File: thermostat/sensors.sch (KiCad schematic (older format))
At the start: 8 parts

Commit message: Moved I2C peripherals into one schematic, moved GPIO peripherals onto main schematic.
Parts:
- added C?: 10n, Capacitor_SMD:C_0603_1608Metric, symbol Device:C
- added R? (x2): 4k7, symbol Device:R
- added U?: AT24C512, Package_DIP:DIP-8_W7.62mm_SMDSocket_SmallPads, symbol Memory_EEPROM:CAT24C256
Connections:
- wire segments 44 -> 71
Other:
- note added: "EEPROM for off-ESP config"
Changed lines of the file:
@@
 $Descr A4 11693 8268
 encoding utf-8
-Sheet 4 4
+Sheet 3 4
 Title ""
 Date ""
@@
 MKW41Z also has RTC but no battery backup for power loss.\nWe do not need interrupt out since MKW41Z has that in its own RTC\n
 NoConn ~ 4050 3700
-Text HLabel 4150 5150 0    50   Input ~ 0
+Text HLabel 4100 5700 0    50   Input ~ 0
 SCL
-Text HLabel 4150 5250 0    50   Input ~ 0
+Text HLabel 4100 5800 0    50   Input ~ 0
 SDA
-Wire Wire Line
-	4150 5150 4350 5150
-Wire Wire Line
-	4350 5250 4150 5250
-Text Label 4350 5150 2    50   ~ 0
+Text Label 5250 5700 2    50   ~ 0
 SCL
-Text Label 4350 5250 2    50   ~ 0
+Text Label 5250 5800 2    50   ~ 0
 SDA
+$Comp
+L Memory_EEPROM:CAT24C256 U?
+U 1 1 5F42FF23
+P 10000 4200
+AR Path="/5F42FF23" Ref="U?"  Part="1"
+AR Path="/5F32546C/5F42FF23" Ref="U?"  Part="1"
+F 0 "U?" H 9750 4450 50  0000 C CNN
+F 1 "AT24C512" H 10250 4450 50  0000 C CNN
+F 2 "Package_DIP:DIP-8_W7.62mm_SMDSocket_SmallPads" H 10000 4200 50  0001 C CNN
+F 3 "https://www.onsemi.cn/PowerSolutions/document/CAT24C256-D.PDF" H 10000 4200 50  0001 C CNN
+	1    10000 4200
+	1    0    0    -1
+$EndComp
+$Comp
+L Device:C C?
+U 1 1 5F42FF29
+P 9750 3800
+AR Path="/5F42FF29" Ref="C?"  Part="1"
+AR Path="/5F32546C/5F42FF29" Ref="C?"  Part="1"
+F 0 "C?" V 9498 3800 50  0000 C CNN
+F 1 "10n" V 9589 3800 50  0000 C CNN
+F 2 "Capacitor_SMD:C_0603_1608Metric" H 9788 3650 50  0001 C CNN
+F 3 "~" H 9750 3800 50  0001 C CNN
+	1    9750 3800
+	0    1    1    0
+$EndComp
+$Comp
+L power:+3V3 #PWR?
+U 1 1 5F42FF2F
+P 10000 3700
+AR Path="/5F42FF2F" Ref="#PWR?"  Part="1"
+AR Path="/5F32546C/5F42FF2F" Ref="#PWR?"  Part="1"
+F 0 "#PWR?" H 10000 3550 50  0001 C CNN
+F 1 "+3V3" H 10015 3873 50  0000 C CNN
+F 2 "" H 10000 3700 50  0001 C CNN
+F 3 "" H 10000 3700 50  0001 C CNN
+	1    10000 3700
+	1    0    0    -1
+$EndComp
+Wire Wire Line
+	10000 3700 10000 3800
+Wire Wire Line
+	9900 3800 10000 3800
+Connection ~ 10000 3800
+Wire Wire Line
+	10000 3800 10000 3900
+$Comp
+L power:GND #PWR?
+U 1 1 5F42FF39
+P 9550 3800
+AR Path="/5F42FF39" Ref="#PWR?"  Part="1"
+AR Path="/5F32546C/5F42FF39" Ref="#PWR?"  Part="1"
+F 0 "#PWR?" H 9550 3550 50  0001 C CNN
+F 1 "GND" V 9555 3672 50  0000 R CNN
+F 2 "" H 9550 3800 50  0001 C CNN
+F 3 "" H 9550 3800 50  0001 C CNN
+	1    9550 3800
+	0    1    1    0
+$EndComp
+Wire Wire Line
+	9550 3800 9600 3800
+Wire Wire Line
+	9550 4100 9550 4200
+Wire Wire Line
+	9550 4550 10000 4550
+Wire Wire Line
+	10450 4550 10450 4300
+Wire Wire Line
+	10450 4300 10400 4300
+Wire Wire Line
+	10000 4500 10000 4550
+Connection ~ 10000 4550
+Wire Wire Line
+	10000 4550 10450 4550
+Wire Wire Line
+	9550 4100 9600 4100
+Wire Wire Line
+	9600 4200 9550 4200
+Connection ~ 9550 4200
+Wire Wire Line
+	9550 4200 9550 4300
+Wire Wire Line
+	9600 4300 9550 4300
+Connection ~ 9550 4300
+Wire Wire Line
+	9550 4300 9550 4550
+$Comp
+L power:GND #PWR?
+U 1 1 5F42FF4E
+P 10000 4600
+AR Path="/5F42FF4E" Ref="#PWR?"  Part="1"
+AR Path="/5F32546C/5F42FF4E" Ref="#PWR?"  Part="1"
+F 0 "#PWR?" H 10000 4350 50  0001 C CNN
+F 1 "GND" H 10005 4427 50  0000 C CNN
+F 2 "" H 10000 4600 50  0001 C CNN
+F 3 "" H 10000 4600 50  0001 C CNN
+	1    10000 4600
+	1    0    0    -1
+$EndComp
+Wire Wire Line
+	10000 4600 10000 4550
+Text Notes 9450 3450 0    50   ~ 0
+EEPROM for off-ESP config
+Wire Notes Line
+	10600 3300 10600 4850
+Wire Notes Line
+	10600 4850 9200 4850
+Wire Notes Line
+	9200 4850 9200 3300
+Wire Notes Line
+	9200 3300 10600 3300
+Text Label 10550 4100 2    50   ~ 0
+SDA
+Wire Wire Line
+	10550 4100 10400 4100
+Text Label 10550 4200 2    50   ~ 0
+SCL
+Wire Wire Line
+	10550 4200 10400 4200
+$Comp
+L Device:R R?
+U 1 1 5F430FFF
+P 4500 5500
+F 0 "R?" H 4570 5546 50  0000 L CNN
+F 1 "4k7" H 4570 5455 50  0000 L CNN
+F 2 "" V 4430 5500 50  0001 C CNN
+F 3 "~" H 4500 5500 50  0001 C CNN
+	1    4500 5500
+	1    0    0    -1
+$EndComp
+$Comp
+L Device:R R?
+U 1 1 5F431377
+P 4850 5500
+F 0 "R?" H 4920 5546 50  0000 L CNN
+F 1 "4k7" H 4920 5455 50  0000 L CNN
+F 2 "" V 4780 5500 50  0001 C CNN
+F 3 "~" H 4850 5500 50  0001 C CNN
+	1    4850 5500
+	1    0    0    -1
+$EndComp
+Wire Wire Line
+	4100 5700 4500 5700
+Wire Wire Line
+	4100 5800 4850 5800
+Wire Wire Line
+	4500 5650 4500 5700
+Connection ~ 4500 5700
+Wire Wire Line
+	4500 5700 5250 5700
+Wire Wire Line
+	4850 5650 4850 5800
+Connection ~ 4850 5800
+Wire Wire Line
+	4850 5800 5250 5800
+$Comp
+L power:+3V3 #PWR?
+U 1 1 5F436E27
+P 4700 5250
+AR Path="/5E9313E4/5F436E27" Ref="#PWR?"  Part="1"
+AR Path="/5F436E27" Ref="#PWR?"  Part="1"
+AR Path="/5F32546C/5F436E27" Ref="#PWR?"  Part="1"
+F 0 "#PWR?" H 4700 5100 50  0001 C CNN
+F 1 "+3V3" H 4715 5423 50  0000 C CNN
+F 2 "" H 4700 5250 50  0001 C CNN
+F 3 "" H 4700 5250 50  0001 C CNN
+	1    4700 5250
+	1    0    0    -1
+$EndComp
+Wire Wire Line
+	4500 5350 4500 5300
+Wire Wire Line
+	4500 5300 4700 5300
+Wire Wire Line
+	4850 5300 4850 5350
+Wire Wire Line
+	4700 5250 4700 5300
+Connection ~ 4700 5300
+Wire Wire Line
+	4700 5300 4850 5300
 $EndSCHEMATC

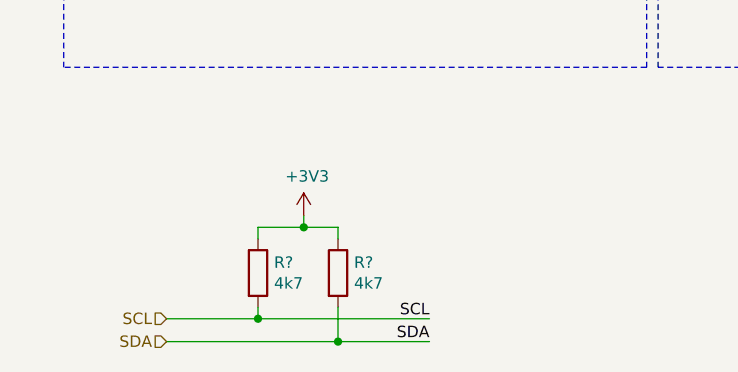
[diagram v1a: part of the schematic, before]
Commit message: Put LEDs and GPIOs into separate schematic, GPIO for arrow buttons are now attached over an expander.
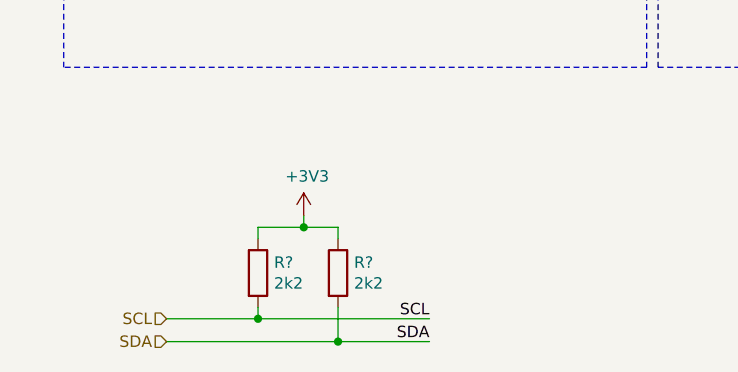
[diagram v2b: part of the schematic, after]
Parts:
- R? (x2): value 4k7 -> 2k2
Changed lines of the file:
@@
 $Descr A4 11693 8268
 encoding utf-8
-Sheet 3 4
+Sheet 3 5
 Title ""
 Date ""
@@
 P 4500 5500
 F 0 "R?" H 4570 5546 50  0000 L CNN
-F 1 "4k7" H 4570 5455 50  0000 L CNN
+F 1 "2k2" H 4570 5455 50  0000 L CNN
 F 2 "" V 4430 5500 50  0001 C CNN
 F 3 "~" H 4500 5500 50  0001 C CNN
@@
 P 4850 5500
 F 0 "R?" H 4920 5546 50  0000 L CNN
-F 1 "4k7" H 4920 5455 50  0000 L CNN
+F 1 "2k2" H 4920 5455 50  0000 L CNN
 F 2 "" V 4780 5500 50  0001 C CNN
 F 3 "~" H 4850 5500 50  0001 C CNN

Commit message: Fixed orphaned symbols after Kicad library update. Kinetis MCU is now in upstream, thanks to me :)
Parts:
- removed U?: MCP7940N-xMS, Package_SO:MSOP-8_3x3mm_P0.65mm, symbol Timer:MCP7940N-xMS
- added U?: MCP7940N-xMS, symbol Timer_RTC:MCP7940N-xMS
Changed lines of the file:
@@
 	6950 2950 6950 3050
-$Comp
-L Timer:MCP7940N-xMS U?
-U 1 1 5F32A0E7
-P 4450 3600
-AR Path="/5F32A0E7" Ref="U?"  Part="1"
-AR Path="/5F32546C/5F32A0E7" Ref="U?"  Part="1"
-F 0 "U?" H 4150 3250 50  0000 C CNN
-F 1 "MCP7940N-xMS" H 4800 3250 50  0000 C CNN
-F 2 "Package_SO:MSOP-8_3x3mm_P0.65mm" H 4450 3600 50  0001 C CNN
-F 3 "http://ww1.microchip.com/downloads/en/DeviceDoc/20005010F.pdf" H 4450 3600 50  0001 C CNN
-	1    4450 3600
-	1    0    0    -1
-$EndComp
 $Comp
 L Sensor_Temperature:MCP9844x-xMN U?
@@
 Wire Wire Line
 	4700 5300 4850 5300
+$Comp
+L Timer_RTC:MCP7940N-xMS U?
+U 1 1 5F69CF88
+P 4450 3600
+F 0 "U?" H 4200 3250 50  0000 C CNN
+F 1 "MCP7940N-xMS" H 4800 3250 50  0000 C CNN
+F 2 "" H 4450 3600 50  0001 C CNN
+F 3 "http://ww1.microchip.com/downloads/en/DeviceDoc/20005010F.pdf" H 4450 3600 50  0001 C CNN
+	1    4450 3600
+	1    0    0    -1
+$EndComp
 $EndSCHEMATC

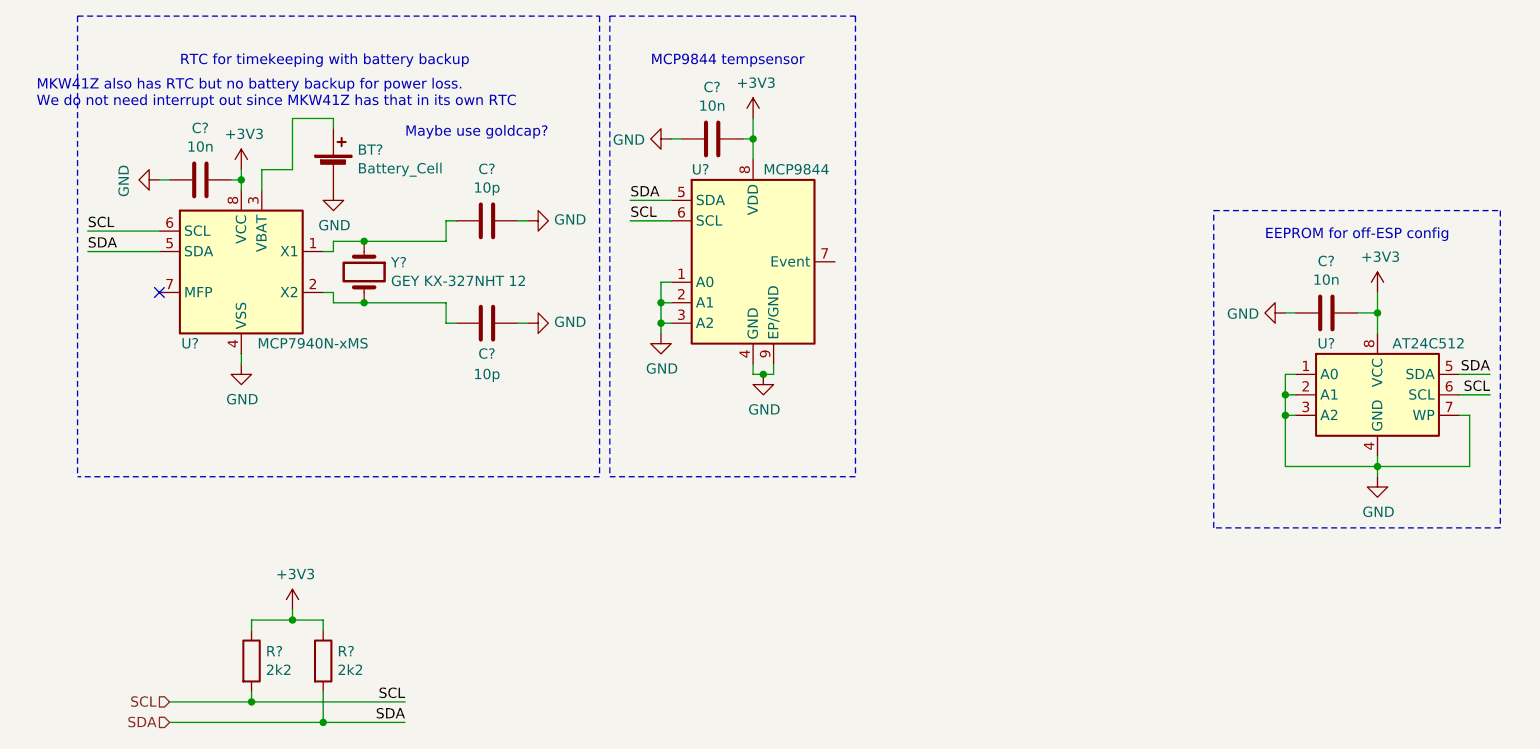
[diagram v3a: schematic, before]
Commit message: Updated symbols after library update, some footprints still need to be assigned. Deleted PCB except for Display and buttons. Button arrangement wrong. Move buttons to other side of Display. Maybe put buttons on separate PCB and create one PCB for MCU and logic, since that needs to be a four layer one. That is expensive and should be kept as small as possible.
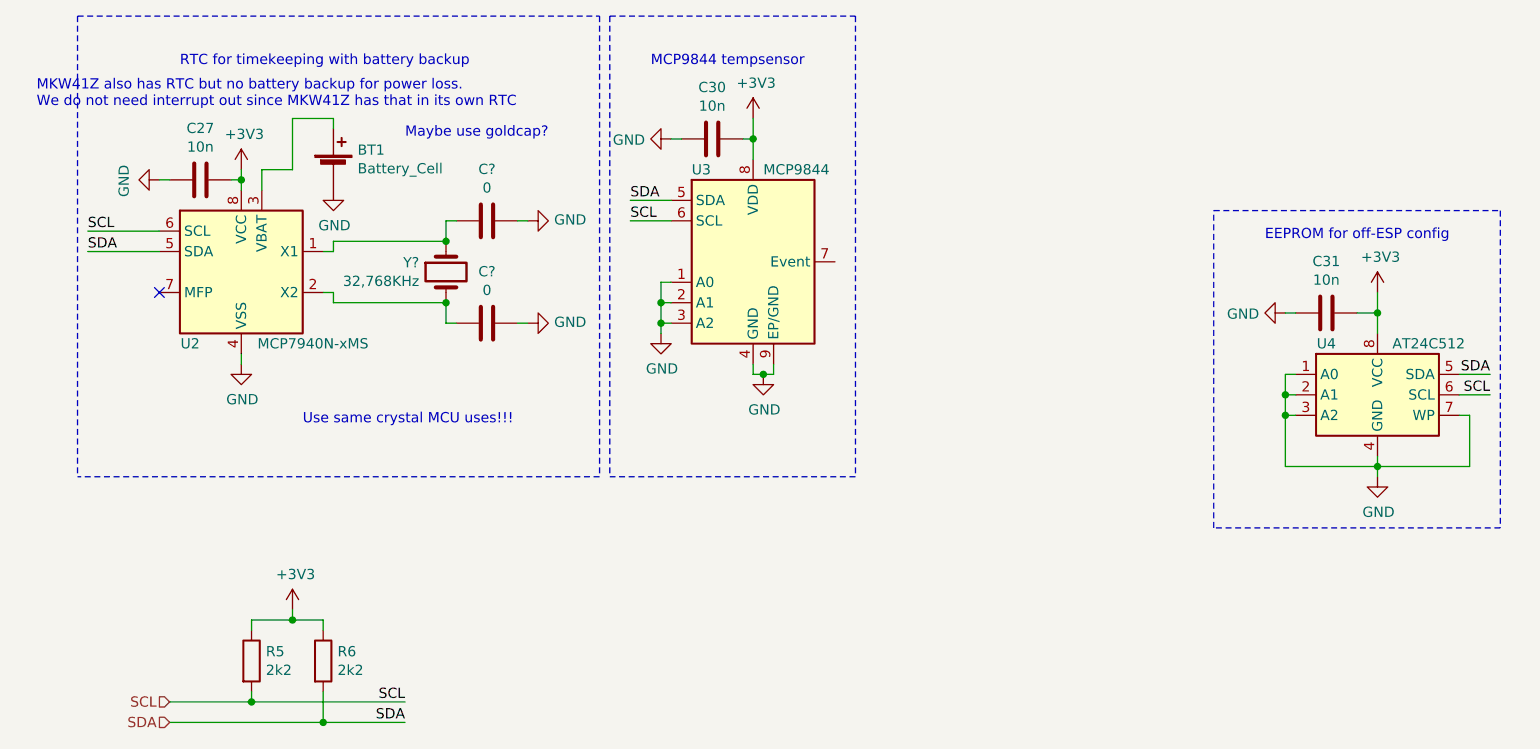
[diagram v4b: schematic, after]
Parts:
- removed C? (x2): 10p, Capacitor_SMD:C_0603_1608Metric, symbol Device:C
- removed Y?: GEY KX-327NHT 12, Crystal:Crystal_SMD_3215-2Pin_3.2x1.5mm, symbol Device:Crystal
- added C? (x2): 0, Capacitor_SMD:C_0603_1608Metric, symbol Device:C
- added Y?: 32,768KHz, symbol Device:Crystal
- R5, R6: renamed from R?; footprint (none) -> Resistor_SMD:R_0603_1608Metric
- U2: renamed from U?; footprint (none) -> Package_SO:MSOP-8_3x3mm_P0.65mm
- gave numbers to parts that had none: 6
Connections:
- net GND: now also C?.1, C?.1
- net at U2.1 (X1): now also C?.2, Y?.1
- net at U2.2 (X2): now also C?.2, Y?.2
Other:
- note added: "Use same crystal MCU uses!!!"

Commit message: Finalized Thermostat circuit based on the MKW41Z.
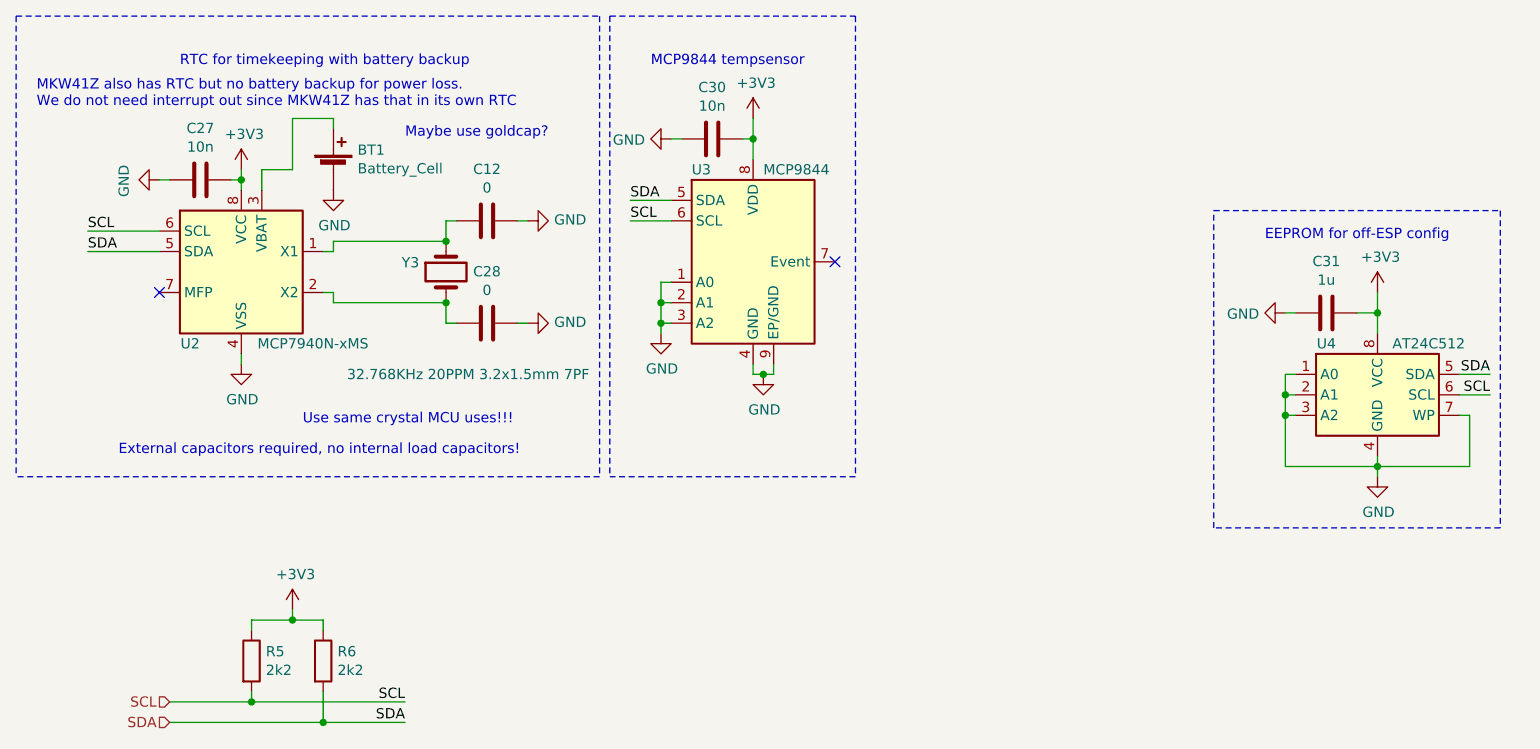
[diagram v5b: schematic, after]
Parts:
- C31: value 10n -> 1u
- Y3: renamed from Y?; value 32,768KHz -> 32.768KHz 20PPM 3.2x1.5mm 7PF; footprint (none) -> Crystal:Crystal_SMD_3215-2Pin_3.2x1.5mm
- gave numbers to parts that had none: 2
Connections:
- no-connect marks 1 -> 2
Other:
- note added: "External capacitors required, no internal load capacitors!"
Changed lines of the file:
@@
 RTC for timekeeping with battery backup
 Wire Notes Line
-	3650 2350 6200 2350
+	3350 2350 6200 2350
 Wire Notes Line
 	6200 2350 6200 4600
@@
 	6250 2350 6250 4600
 Wire Notes Line
-	3650 2350 3650 4600
-Wire Notes Line
-	6200 4600 3650 4600
+	3350 2350 3350 4600
+Wire Notes Line
+	6200 4600 3350 4600
 $Comp
 L Device:C C?
@@
 AR Path="/5F32546C/5F42FF29" Ref="C31"  Part="1"
 F 0 "C31" V 9498 3800 50  0000 C CNN
-F 1 "10n" V 9589 3800 50  0000 C CNN
+F 1 "1u" V 9589 3800 50  0000 C CNN
 F 2 "Capacitor_SMD:C_0603_1608Metric" H 9788 3650 50  0001 C CNN
 F 3 "~" H 9750 3800 50  0001 C CNN
@@
 P 5450 3600
 AR Path="/5F6FEFA4" Ref="Y?"  Part="1"
-AR Path="/5F32546C/5F6FEFA4" Ref="Y?"  Part="1"
-F 0 "Y?" V 5404 3731 50  0000 L CNN
-F 1 "32,768KHz" V 5495 3731 50  0000 L CNN
-F 2 "" H 5450 3600 50  0001 C CNN
+AR Path="/5F32546C/5F6FEFA4" Ref="Y3"  Part="1"
+F 0 "Y3" V 5404 3731 50  0000 L CNN
+F 1 "32.768KHz 20PPM 3.2x1.5mm 7PF" V 5950 2900 50  0000 L CNN
+F 2 "Crystal:Crystal_SMD_3215-2Pin_3.2x1.5mm" H 5450 3600 50  0001 C CNN
 F 3 "~" H 5450 3600 50  0001 C CNN
 	1    5450 3600
@@
 P 5650 3350
 AR Path="/5F70128F" Ref="C?"  Part="1"
-AR Path="/5F32546C/5F70128F" Ref="C?"  Part="1"
-F 0 "C?" V 5398 3350 50  0000 C CNN
+AR Path="/5F32546C/5F70128F" Ref="C12"  Part="1"
+F 0 "C12" V 5398 3350 50  0000 C CNN
 F 1 "0" V 5489 3350 50  0000 C CNN
 F 2 "Capacitor_SMD:C_0603_1608Metric" H 5688 3200 50  0001 C CNN
@@
 P 5650 3850
 AR Path="/5F701687" Ref="C?"  Part="1"
-AR Path="/5F32546C/5F701687" Ref="C?"  Part="1"
-F 0 "C?" V 5398 3850 50  0000 C CNN
+AR Path="/5F32546C/5F701687" Ref="C28"  Part="1"
+F 0 "C28" V 5398 3850 50  0000 C CNN
 F 1 "0" V 5489 3850 50  0000 C CNN
 F 2 "Capacitor_SMD:C_0603_1608Metric" H 5688 3700 50  0001 C CNN
@@
 	0    1    1    0
 $EndComp
+Text Notes 3850 4500 0    50   ~ 0
+External capacitors required, no internal load capacitors!
+NoConn ~ 7350 3550
 $EndSCHEMATC

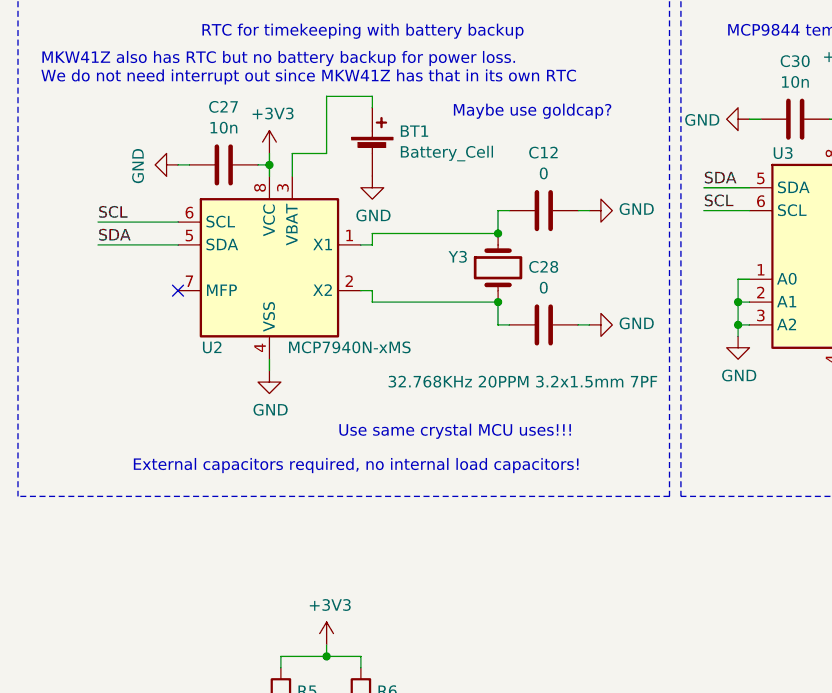
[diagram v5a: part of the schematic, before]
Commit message: Replaced DCDC input cap as the package was way too small for the required capacitance, started working on the BOM and looking up parts on Mouser. Need to replace input Molex connector as it is not in stock at Mouser. Easiest is solder pads (I will have a connector on the other side of the cable anyway...) or just the same connector but with higher pincount that Mouser has in stock
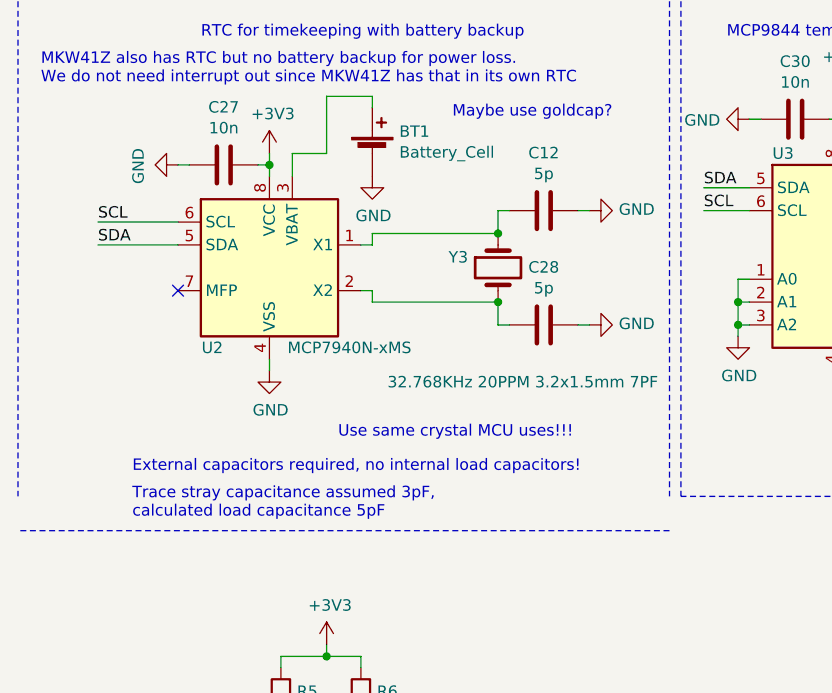
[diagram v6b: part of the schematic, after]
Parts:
- C12, C28: value 0 -> 5p
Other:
- note added: "Trace stray capacitance assumed 3pF,\ncalculated load capacitance 5pF"
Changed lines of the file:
@@
 	3350 2350 3350 4600
 Wire Notes Line
-	6200 4600 3350 4600
+	6200 4750 3350 4750
 $Comp
 L Device:C C?
@@
 AR Path="/5F32546C/5F70128F" Ref="C12"  Part="1"
 F 0 "C12" V 5398 3350 50  0000 C CNN
-F 1 "0" V 5489 3350 50  0000 C CNN
+F 1 "5p" V 5489 3350 50  0000 C CNN
 F 2 "Capacitor_SMD:C_0603_1608Metric" H 5688 3200 50  0001 C CNN
 F 3 "~" H 5650 3350 50  0001 C CNN
@@
 AR Path="/5F32546C/5F701687" Ref="C28"  Part="1"
 F 0 "C28" V 5398 3850 50  0000 C CNN
-F 1 "0" V 5489 3850 50  0000 C CNN
+F 1 "5p" V 5489 3850 50  0000 C CNN
 F 2 "Capacitor_SMD:C_0603_1608Metric" H 5688 3700 50  0001 C CNN
 F 3 "~" H 5650 3850 50  0001 C CNN
@@
 External capacitors required, no internal load capacitors!
 NoConn ~ 7350 3550
+Text Notes 3850 4700 0    50   ~ 0
+Trace stray capacitance assumed 3pF,\ncalculated load capacitance 5pF
 $EndSCHEMATC

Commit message: Changed Button lines to MKW41 pins that also have LLWU interrupt capabilities. It will never get there, but who knows what the future brings.
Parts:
- U2: symbol Timer_RTC:MCP7940N-xMS -> home-thermostat-rescue:MCP7940N-xMS-Timer_RTC
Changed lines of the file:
@@
 	4700 5300 4850 5300
 $Comp
-L Timer_RTC:MCP7940N-xMS U2
+L home-thermostat-rescue:MCP7940N-xMS-Timer_RTC U2
 U 1 1 5F69CF88
 P 4450 3600
